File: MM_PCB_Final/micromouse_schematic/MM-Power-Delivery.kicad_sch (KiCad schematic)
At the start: 6 parts, among them J7 JST Connector, J8 JST Connector, U8 Voltage Regulator

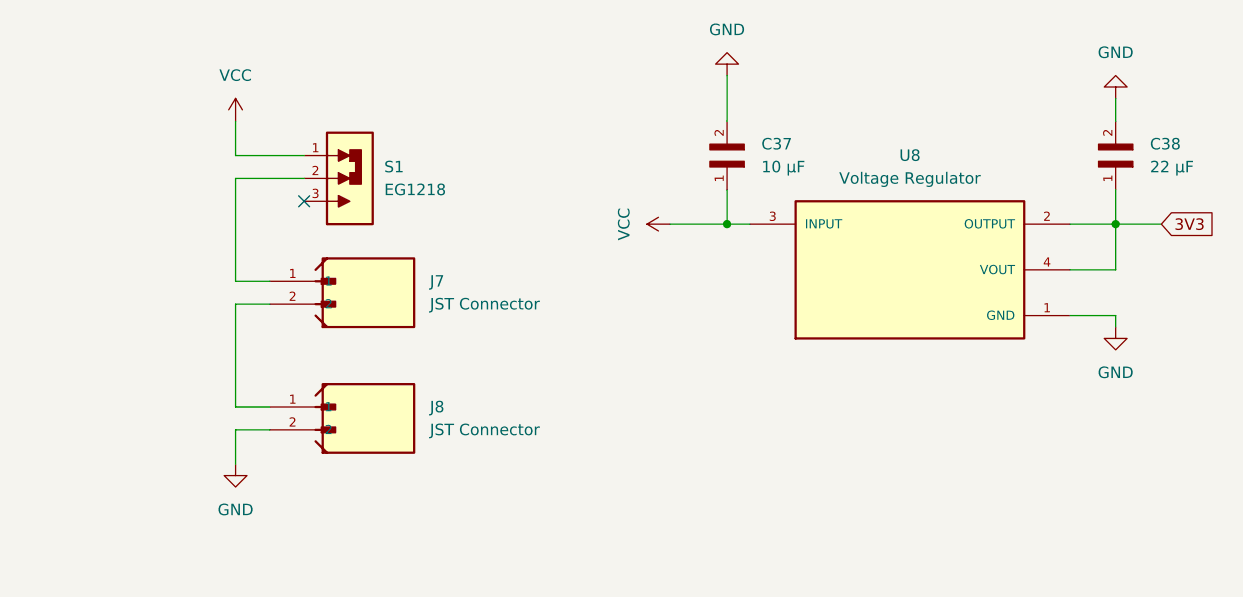
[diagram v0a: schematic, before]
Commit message: fix mgnd and gnd short
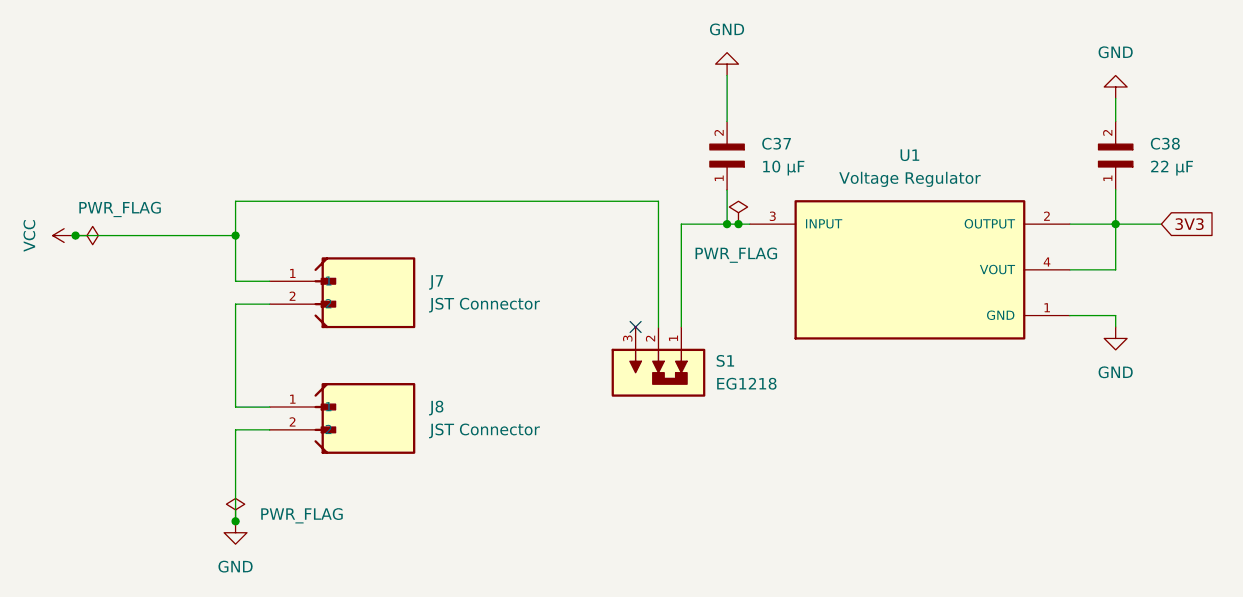
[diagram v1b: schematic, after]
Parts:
- removed U8: Voltage Regulator, Voltage_Regulator_AZ1117IH-3.3TRG1:SOT230P700X185-4N, symbol VoltageRegulator_AZ1117IH-3.3TRG1:AZ1117IH-3.3TRG1
- added U1: Voltage Regulator, AZ1117IH-3.3TRG1:SOT230P700X185-4N, symbol VoltageRegulator_AZ1117IH-3.3TRG1:AZ1117IH-3.3TRG1
- C37: footprint Ceramic_Capacitor_10uF_GRM21BC81C106KA73L:CAPC2012X140N -> CL21B106KOQNNNE:CAPC2012X140N
- C38: footprint Ceramic_Capacitor_22uF_CL21A226KPCLRNC:CAPC2012X95N -> CL21A226MPQNNNE:CAPC2012X140N
- J7, J8: footprint JST_Connector_B2B-PH-K-S:JST_B2B-PH-K-S -> B2B_PH_K_S:JST_B2B-PH-K-S
- S1: footprint Slide_Switch_EG1218:SW_EG1218 -> EG1218:SW_EG1218
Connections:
- net 3V3: now also U1.2 (OUTPUT), U1.4 (VOUT)
- net GND: now also U1.1 (GND)
- net VCC: now also J7.1, S1.2; no longer C37.1, S1.1
- new net: C37.1, S1.1, U1.3 (INPUT)
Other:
- moved on the sheet: S1
